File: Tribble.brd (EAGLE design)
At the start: 154.5 x 47.2 mm, 119 parts, among them J1 10118193-0001LF, J2 68602-406HLF, J3 SJ1-2503A, J4 RJHSE-5381, J5 SJ1-2503A, J6 SJ1-2503A, J7 HFW6R-2STE1LF, P1 TC33X-2, U1 AT90USB646-MU, U10 IP4234CZ6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

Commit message: updated the BOM info for Tribble Rev 7
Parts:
- CG1, CG10, CG2, CG3, CG4, CG5, CG6, CG7, CG8, CG9: value CG0402MLC-05LG -> B72590D50H260
- D3: value PMEG3010BER,115 -> PMEG6010EP,115; device PP_Passives:SOD-123 -> PP_Passives:SOD-128
- U1: value AT90USB646-MU -> AT90USB1287-MU
- U11: value AT90USB646-AU -> AT90USB1287-AU
- U12: value FDS6681Z -> FDS6679AZ
- X1: value CX3225SB16000D0FLJZZ -> TSX-3225 16.0000MF10U-B0
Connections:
- net N$14: now also D3.CATHODE; no longer D3.1
- net V_USB: now also D3.ANODE; no longer D3.2
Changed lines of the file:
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@@
 <attribute name="NAME" x="-73.21" y="17.33" size="0.8128" layer="25" font="vector"/>
 </element>
-<element name="X1" library="kyocera-crystals" package="3.2X2.5MM" value="CX3225SB16000D0FLJZZ" x="-21.5" y="3" smashed="yes" rot="R135">
+<element name="X1" library="kyocera-crystals" package="3.2X2.5MM" value="TSX-3225 16.0000MF10U-B0" x="-21.5" y="3" smashed="yes" rot="R135">
 <attribute name="NAME" x="-22.112025" y="1.7086875" size="0.8128" layer="25" rot="R315"/>
 </element>
@@
 <attribute name="NAME" x="33.5" y="17.95" size="0.8128" layer="25" font="vector"/>
 </element>
-<element name="CG2" library="parkers_parts" package="0402_RES" value="CG0402MLC-05LG" x="30" y="8" smashed="yes" rot="R90">
+<element name="CG2" library="parkers_parts" package="0402_RES" value="B72590D50H260" x="30" y="8" smashed="yes" rot="R90">
 <attribute name="NAME" x="29.011" y="5.9485" size="0.8128" layer="25" font="vector"/>
 </element>
-<element name="CG3" library="parkers_parts" package="0402_RES" value="CG0402MLC-05LG" x="32" y="8" smashed="yes" rot="R90">
+<element name="CG3" library="parkers_parts" package="0402_RES" value="B72590D50H260" x="32" y="8" smashed="yes" rot="R90">
 <attribute name="NAME" x="32.761" y="7.6985" size="0.8128" layer="25" font="vector"/>
 </element>
@@
 <attribute name="NAME" x="3.011" y="-15.3015" size="0.8128" layer="25" font="vector"/>
 </element>
-<element name="CG5" library="parkers_parts" package="0402_RES" value="CG0402MLC-05LG" x="-31.25" y="6.75" smashed="yes" rot="R270">
+<element name="CG5" library="parkers_parts" package="0402_RES" value="B72590D50H260" x="-31.25" y="6.75" smashed="yes" rot="R270">
 <attribute name="NAME" x="-30.489" y="6.9485" size="0.8128" layer="25" font="vector"/>
 </element>
-<element name="CG6" library="parkers_parts" package="0402_RES" value="CG0402MLC-05LG" x="-39" y="7.25" smashed="yes" rot="R90">
+<element name="CG6" library="parkers_parts" package="0402_RES" value="B72590D50H260" x="-39" y="7.25" smashed="yes" rot="R90">
 <attribute name="NAME" x="-39.739" y="8.4485" size="0.8128" layer="25" font="vector"/>
 </element>
@@
 <attribute name="NAME" x="-31.739" y="-4.0515" size="0.8128" layer="25" font="vector"/>
 </element>
-<element name="U11" library="at90usb" package="TQFP64" value="AT90USB646-AU" x="-13" y="-7" smashed="yes" rot="R225"/>
+<element name="U11" library="at90usb" package="TQFP64" value="AT90USB1287-AU" x="-13" y="-7" smashed="yes" rot="R225"/>
 <element name="R22" library="parkers_parts" package="0402_RES" value="0" x="26.5" y="11.75" smashed="yes" rot="R270">
 <attribute name="NAME" x="25.511" y="12.9485" size="0.8128" layer="25" font="vector"/>
@@
 <attribute name="NAME" x="16.011" y="-11.3015" size="0.8128" layer="25" font="vector"/>
 </element>
-<element name="U1" library="at90usb" package="MLF64" value="AT90USB646-MU" x="-13" y="-7" smashed="yes" rot="R225">
+<element name="U1" library="at90usb" package="MLF64" value="AT90USB1287-MU" x="-13" y="-7" smashed="yes" rot="R225">
 <attribute name="NAME" x="-2.940303125" y="-6.770565625" size="0.8128" layer="25" font="vector" rot="R315"/>
 </element>
@@
 <attribute name="NAME" x="-58" y="-3.75" size="0.8128" layer="25" font="vector"/>
 </element>
-<element name="CG4" library="parkers_parts" package="0402_RES" value="CG0402MLC-05LG" x="-34.75" y="-9.5" smashed="yes" rot="R270">
+<element name="CG4" library="parkers_parts" package="0402_RES" value="B72590D50H260" x="-34.75" y="-9.5" smashed="yes" rot="R270">
 <attribute name="NAME" x="-34.989" y="-11.5515" size="0.8128" layer="25" font="vector"/>
 </element>
-<element name="CG7" library="parkers_parts" package="0402_RES" value="CG0402MLC-05LG" x="-37.5" y="-12" smashed="yes">
+<element name="CG7" library="parkers_parts" package="0402_RES" value="B72590D50H260" x="-37.5" y="-12" smashed="yes">
 <attribute name="NAME" x="-36.511" y="-12.6985" size="0.8128" layer="25" font="vector" rot="R180"/>
 </element>
-<element name="CG1" library="parkers_parts" package="0402_RES" value="CG0402MLC-05LG" x="-40.75" y="4.5" smashed="yes" rot="R180">
+<element name="CG1" library="parkers_parts" package="0402_RES" value="B72590D50H260" x="-40.75" y="4.5" smashed="yes" rot="R180">
 <attribute name="NAME" x="-44.239" y="4.1985" size="0.8128" layer="25" font="vector"/>
 </element>
@@
 <attribute name="NAME" x="13" y="17.8" size="0.8128" layer="25" font="vector"/>
 </element>
-<element name="CG8" library="parkers_parts" package="0402_RES" value="CG0402MLC-05LG" x="15.249996875" y="10.250003125" smashed="yes" rot="R90">
+<element name="CG8" library="parkers_parts" package="0402_RES" value="B72590D50H260" x="15.249996875" y="10.250003125" smashed="yes" rot="R90">
 <attribute name="NAME" x="14.261003125" y="11.698503125" size="0.8128" layer="25" font="vector"/>
 </element>
-<element name="CG9" library="parkers_parts" package="0402_RES" value="CG0402MLC-05LG" x="13.999996875" y="10.250003125" smashed="yes" rot="R90">
+<element name="CG9" library="parkers_parts" package="0402_RES" value="B72590D50H260" x="13.999996875" y="10.250003125" smashed="yes" rot="R90">
 <attribute name="NAME" x="13.011003125" y="7.948503125" size="0.8128" layer="25" font="vector"/>
 </element>
@@
 <attribute name="NAME" x="58.48900625" y="-14.5515" size="0.8128" layer="26" font="vector" rot="MR0"/>
 </element>
-<element name="CG10" library="parkers_parts" package="0402_RES" value="CG0402MLC-05LG" x="19.25" y="6.25" smashed="yes" rot="R270">
+<element name="CG10" library="parkers_parts" package="0402_RES" value="B72590D50H260" x="19.25" y="6.25" smashed="yes" rot="R270">
 <attribute name="NAME" x="15.761" y="5.4485" size="0.8128" layer="25" font="vector"/>
 </element>
@@
 </element>
 <element name="R36" library="PP_Passives" package="1206" value="LRF1206-LF-R006JT" x="17" y="-24" rot="MR180"/>
-<element name="U12" library="PP_DiscreteSemi" package="DSO-8" value="FDS6681Z" x="-61.750003125" y="0.5"/>
+<element name="U12" library="PP_DiscreteSemi" package="DSO-8" value="FDS6679AZ" x="-61.750003125" y="0.5"/>
 <element name="R37" library="parkers_parts" package="0402_RES" value="10K" x="-59.750003125" y="-4.5" smashed="yes" rot="R180">
 <attribute name="NAME" x="-57.989003125" y="-4.8015" size="0.8128" layer="25" font="vector"/>
@@
 <attribute name="NAME" x="19.761" y="7.3235" size="0.8128" layer="25" font="vector"/>
 </element>
-<element name="D3" library="PP_Passives" package="SOD-123" value="PMEG3010BER,115" x="26.75" y="7" smashed="yes" rot="R90">
+<element name="D3" library="PP_Passives" package="SOD-128" value="PMEG6010EP,115" x="26.75" y="7" smashed="yes" rot="R90">
 <attribute name="NAME" x="28" y="8.7" size="0.8128" layer="25" font="vector"/>
 </element>
@@
 <contactref element="U11" pad="8"/>
 <contactref element="U10" pad="5"/>
-<contactref element="D3" pad="2"/>
+<contactref element="D3" pad="ANODE"/>
 <wire x1="22.05" y1="15.46" x2="22.05" y2="12.7" width="0.254" layer="1"/>
 <wire x1="22.05" y1="12.7" x2="23.25" y2="11.5" width="0.254" layer="1"/>
@@
 <wire x1="24" y1="9" x2="23.75" y2="9" width="0.254" layer="1"/>
 <wire x1="23.75" y1="9" x2="23" y2="9.75" width="0.254" layer="1"/>
-<wire x1="26.75" y1="8.73" x2="25.98" y2="9" width="0.254" layer="1"/>
+<wire x1="26.75" y1="9.2" x2="25.98" y2="9" width="0.254" layer="1"/>
 <wire x1="25.98" y1="9" x2="24" y2="9" width="0.254" layer="1"/>
 <contactref element="U16" pad="3"/>
@@
 </signal>
 <signal name="N$14">
-<contactref element="D3" pad="1"/>
+<contactref element="D3" pad="CATHODE"/>
 <contactref element="F2" pad="1"/>
 <wire x1="24.42" y1="4.4" x2="24.25" y2="4.4" width="0.254" layer="1"/>
 <wire x1="24.42" y1="4.4" x2="24.25" y2="4.4" width="0.3048" layer="1"/>
-<wire x1="26.75" y1="5.73" x2="25.58" y2="5.73" width="0.3048" layer="1"/>
-<wire x1="25.58" y1="5.73" x2="24.25" y2="4.4" width="0.3048" layer="1"/>
+<wire x1="24.58" y1="4.73" x2="24.25" y2="4.4" width="0.3048" layer="1"/>
+<wire x1="26.75" y1="4.8" x2="24.25" y2="4.8" width="0.254" layer="1"/>
+<wire x1="24.25" y1="4.8" x2="24.25" y2="4.4" width="0.254" layer="1"/>
 </signal>
 <signal name="PE7">
@@
 </signal>
 </signals>
-<errors>
-</errors>
 </board>
 </drawing>

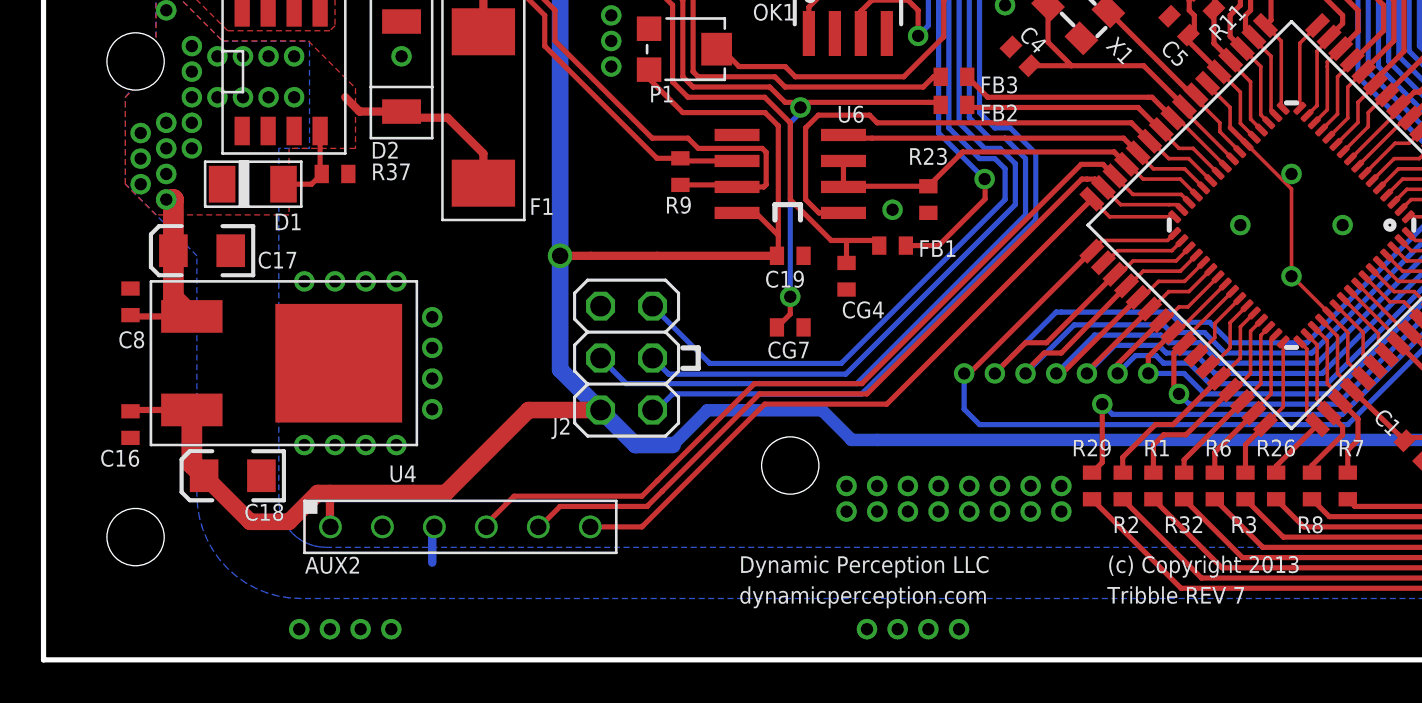
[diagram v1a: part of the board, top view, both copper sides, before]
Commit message: Fixed the issues for Tribble that popped up during EMC testing
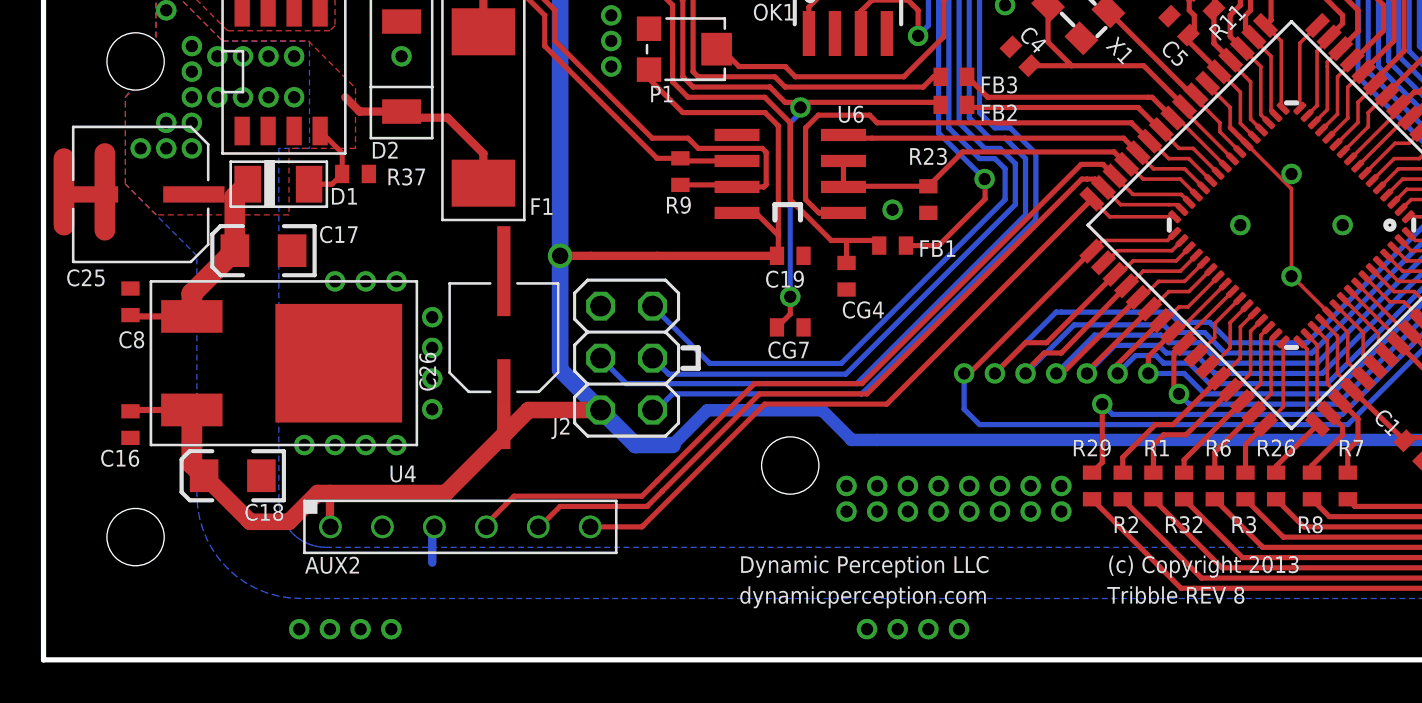
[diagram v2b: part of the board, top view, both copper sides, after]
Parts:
- added C25: 100uF, PP_Passives:6.3MM_CAP_SMD
- added C26: 100uF, PP_Passives:5MM_CAP_SMD
- FB1, FB2, FB3: value LI0402C470R-10 -> HZ0402B102R-10
- moved C17 3.00 mm to (-63.3, -8.25)
- moved D1 1.25 mm to (-62.8, -5.00)
- moved R37 1.00 mm to (-58.8, -4.50)
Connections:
- net +5V: now also C26.P
- net GND: now also C25.NEG, C26.N
- net VIN: now also C25.POS
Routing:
- net GND: track 30.6 -> 37.6 mm, vias 82 -> 81
- net +5V: track 436.6 -> 438.0 mm
- net VIN: track 41.0 -> 42.1 mm, vias 22 -> 18
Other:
- board text added: "Tribble REV 8"
- board text removed: "Tribble REV 7"

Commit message: tagged loads of PCBs and made sure BOMs where up to date
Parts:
- added D4: P6SMB30CAT3G, PP_Passives:DO-214AA
- added TVS1, TVS2, TVS3, TVS4: ESD11B5.0ST5G, PP_Passives:DSN-2
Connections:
- net +5V: now also TVS1.P$2, TVS2.P$2, TVS3.P$2, TVS4.P$2
- net GND: now also D4.A, TVS1.P$1, TVS2.P$1, TVS3.P$1, TVS4.P$1
- net VIN_J: now also D4.C
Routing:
- net GND: track 37.6 -> 44.1 mm
- net VIN_J: track 0.00 -> 5.94 mm
- net +5V: track 438.0 -> 441.1 mm
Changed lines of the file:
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@@
 <element name="C5" library="parkers_parts" package="0402_CAP" value=".1uF" x="-18.5" y="2.75" rot="R135"/>
 <element name="C6" library="parkers_parts" package="0402_CAP" value=".1uF" x="-0.25" y="-10.5" smashed="yes" rot="R315">
-<attribute name="NAME" x="-0.308965625" y="-9.453203125" size="0.8128" layer="25" font="vector" rot="R315"/>
+<attribute name="NAME" x="-1.058965625" y="-8.953203125" size="0.8128" layer="25" font="vector" rot="R315"/>
 </element>
 <element name="R5" library="parkers_parts" package="0402_RES" value="20K" x="14.5" y="-12.25" smashed="yes">
@@
 </element>
 <element name="C26" library="PP_Passives" package="5MM_CAP_SMD" value="100uF" x="-51.5" y="-12.5" rot="R90"/>
+<element name="TVS1" library="PP_Passives" package="DSN-2" value="ESD11B5.0ST5G" x="-18.5" y="5.5"/>
+<element name="TVS2" library="PP_Passives" package="DSN-2" value="ESD11B5.0ST5G" x="1" y="-9.75" smashed="yes" rot="R90">
+<attribute name="NAME" x="0.78" y="-8.53" size="0.8128" layer="21" font="vector"/>
+</element>
+<element name="TVS3" library="PP_Passives" package="DSN-2" value="ESD11B5.0ST5G" x="-6.75" y="-16.25" smashed="yes" rot="R270">
+<attribute name="NAME" x="-7.22" y="-15.53" size="0.8128" layer="21" font="vector"/>
+</element>
+<element name="TVS4" library="PP_Passives" package="DSN-2" value="ESD11B5.0ST5G" x="-68.25" y="-19" smashed="yes">
+<attribute name="NAME" x="-70.47" y="-20.28" size="0.8128" layer="21" font="vector"/>
+</element>
+<element name="D4" library="PP_Passives" package="DO-214AA" value="P6SMB30CAT3G" x="-61.25" y="7.25" rot="MR90"/>
 </elements>
 <signals>
@@
 <via x="3.81" y="15.5" extent="1-16" drill="0.8"/>
 <wire x1="-0.70961875" y1="-10.040378125" x2="0.080759375" y2="-9.25" width="0.254" layer="1"/>
-<wire x1="0.080759375" y1="-9.25" x2="2.25" y2="-9.25" width="0.254" layer="1"/>
+<wire x1="0.080759375" y1="-9.25" x2="1.25" y2="-9.25" width="0.254" layer="1"/>
 <via x="2.25" y="-9.25" extent="1-16" drill="0.8"/>
+<wire x1="1.25" y1="-9.25" x2="2.25" y2="-9.25" width="0.254" layer="1"/>
 <wire x1="2.25" y1="-9.25" x2="1.25" y2="-9.25" width="0.6096" layer="16"/>
 <wire x1="1.25" y1="-9.25" x2="-4.5" y2="-15" width="0.6096" layer="16"/>
@@
 <wire x1="-0.25" y1="16.75" x2="0" y2="17" width="0.8128" layer="16"/>
 <wire x1="0" y1="17" x2="2.5" y2="17" width="0.8128" layer="16"/>
-<wire x1="-7.45961875" y1="-17.381546875" x2="-5.881546875" y2="-17.381546875" width="0.254" layer="1"/>
+<wire x1="-7.45961875" y1="-17.381546875" x2="-6.75" y2="-17.381546875" width="0.254" layer="1"/>
+<wire x1="-6.75" y1="-17.381546875" x2="-5.881546875" y2="-17.381546875" width="0.254" layer="1"/>
 <wire x1="-5.881546875" y1="-17.381546875" x2="-5.875" y2="-17.375" width="0.254" layer="1"/>
 <via x="-5.875" y="-17.375" extent="1-16" drill="0.6"/>
@@
 <wire x1="4.3" y1="6.9" x2="4.3" y2="11.51" width="0.254" layer="1"/>
 <wire x1="4.3" y1="11.51" x2="3.56" y2="12.25" width="0.254" layer="1"/>
-<wire x1="-18" y1="4" x2="-18" y2="16.75" width="0.254" layer="1"/>
+<wire x1="-18" y1="4" x2="-18" y2="5.5" width="0.254" layer="1"/>
 <via x="-18" y="16.75" extent="1-16" drill="0.6"/>
+<wire x1="-18" y1="5.5" x2="-18" y2="16.75" width="0.254" layer="1"/>
 <wire x1="-18" y1="16.75" x2="-16.75" y2="16.75" width="0.254" layer="16"/>
 <contactref element="R15" pad="1"/>
@@
 <wire x1="60.250003125" y1="1.439340625" x2="60.250003125" y2="-1.75" width="0.254" layer="1"/>
 <wire x1="51.650003125" y1="2.65" x2="51.650003125" y2="3.25" width="0.254" layer="1"/>
-<wire x1="-66.750003125" y1="-16.035" x2="-66.750003125" y2="-18.65" width="1.016" layer="1"/>
+<wire x1="-66.750003125" y1="-16.035" x2="-66.750003125" y2="-18.5" width="1.016" layer="1"/>
+<wire x1="-66.750003125" y1="-18.5" x2="-66.750003125" y2="-18.65" width="1.016" layer="1"/>
 <wire x1="-66.750003125" y1="-18.65" x2="-66.150003125" y2="-19.25" width="1.016" layer="1"/>
 <wire x1="-38.15" y1="-8.5" x2="-44" y2="-8.5" width="0.4064" layer="1"/>
@@
 <wire x1="-51.5" y1="-15.75" x2="-51.5" y2="-16.999996875" width="0.6096" layer="1"/>
 <wire x1="-51.5" y1="-16.999996875" x2="-51.375" y2="-17.124996875" width="0.6096" layer="1"/>
+<contactref element="TVS4" pad="P$2"/>
+<contactref element="TVS1" pad="P$2"/>
+<contactref element="TVS2" pad="P$2"/>
+<contactref element="TVS3" pad="P$2"/>
+<wire x1="-18.265" y1="5.5" x2="-18" y2="5.5" width="0.254" layer="1"/>
+<wire x1="1" y1="-9.515" x2="1" y2="-9.25" width="0.254" layer="1"/>
+<wire x1="1" y1="-9.25" x2="1.25" y2="-9.25" width="0.254" layer="1"/>
+<wire x1="-6.75" y1="-16.485" x2="-6.75" y2="-17.381546875" width="0.254" layer="1"/>
+<wire x1="-68.015" y1="-19" x2="-67.250003125" y2="-19" width="0.254" layer="1"/>
+<wire x1="-67.250003125" y1="-19" x2="-66.750003125" y2="-18.5" width="0.254" layer="1"/>
 </signal>
 <signal name="GND">
@@
 <wire x1="-71" y1="-3.5" x2="-71" y2="-7.25" width="1.016" layer="1"/>
 <contactref element="C25" pad="NEG"/>
+<wire x1="-72.25" y1="-3.75" x2="-72.25" y2="-7" width="1.016" layer="1"/>
+<wire x1="-71.5" y1="-3.75" x2="-71.5" y2="-7" width="1.016" layer="1"/>
+<contactref element="TVS4" pad="P$1"/>
+<contactref element="TVS3" pad="P$1"/>
+<contactref element="TVS2" pad="P$1"/>
+<contactref element="TVS1" pad="P$1"/>
+<contactref element="D4" pad="A"/>
 </signal>
 <signal name="AREF" class="4">
@@
 <vertex x="-59.750003125" y="2.75"/>
 </polygon>
+<contactref element="D4" pad="C"/>
+<wire x1="-61.25" y1="5.04" x2="-63.12" y2="5.04" width="1.27" layer="16"/>
+<wire x1="-63.12" y1="5.04" x2="-66" y2="7.92" width="1.27" layer="16"/>
 </signal>
 <signal name="N$3">

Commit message: Revert to REV 7 of Tribble
Did not need the board fixes in REV 8 of the pcb.
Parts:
- removed C25: 100uF, PP_Passives:6.3MM_CAP_SMD
- removed C26: 100uF, PP_Passives:5MM_CAP_SMD
- removed D4: P6SMB30CAT3G, PP_Passives:DO-214AA
- removed TVS1, TVS2, TVS3, TVS4: ESD11B5.0ST5G, PP_Passives:DSN-2
- FB1, FB2, FB3: value HZ0402B102R-10 -> LI0402C470R-10
- moved C17 3.00 mm to (-66.3, -8.25)
- moved D1 1.25 mm to (-64.0, -5.00)
- moved R37 1.00 mm to (-59.8, -4.50)
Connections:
- net +5V: no longer C26.P, TVS1.P$2, TVS2.P$2, TVS3.P$2, TVS4.P$2
- net GND: no longer C25.NEG, C26.N, D4.A, TVS1.P$1, TVS2.P$1, TVS3.P$1, TVS4.P$1
- net VIN: no longer C25.POS
- net VIN_J: no longer D4.C
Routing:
- net GND: track 44.1 -> 30.6 mm, vias 81 -> 82
- net VIN_J: track 5.94 -> 0.00 mm
- net +5V: track 441.1 -> 436.6 mm
- net VIN: track 42.1 -> 41.0 mm, vias 18 -> 22
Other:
- board text added: "Tribble REV 7"
- board text removed: "Tribble REV 8"
